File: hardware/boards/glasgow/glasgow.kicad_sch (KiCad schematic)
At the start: 95 parts, among them J1 USB_C_USB2.0, SW1 RST, U1 CY7C68013A-56LTX, U15 TPD3S014, U2 CAT24M01X, U3 BL24C256A-SFRC, U30 ICE40HX8K-BG121, U36 TLV73312PQDRVR, U7 APX811-40UG-7, U8 TLV75533PDRVR, Y1 24M

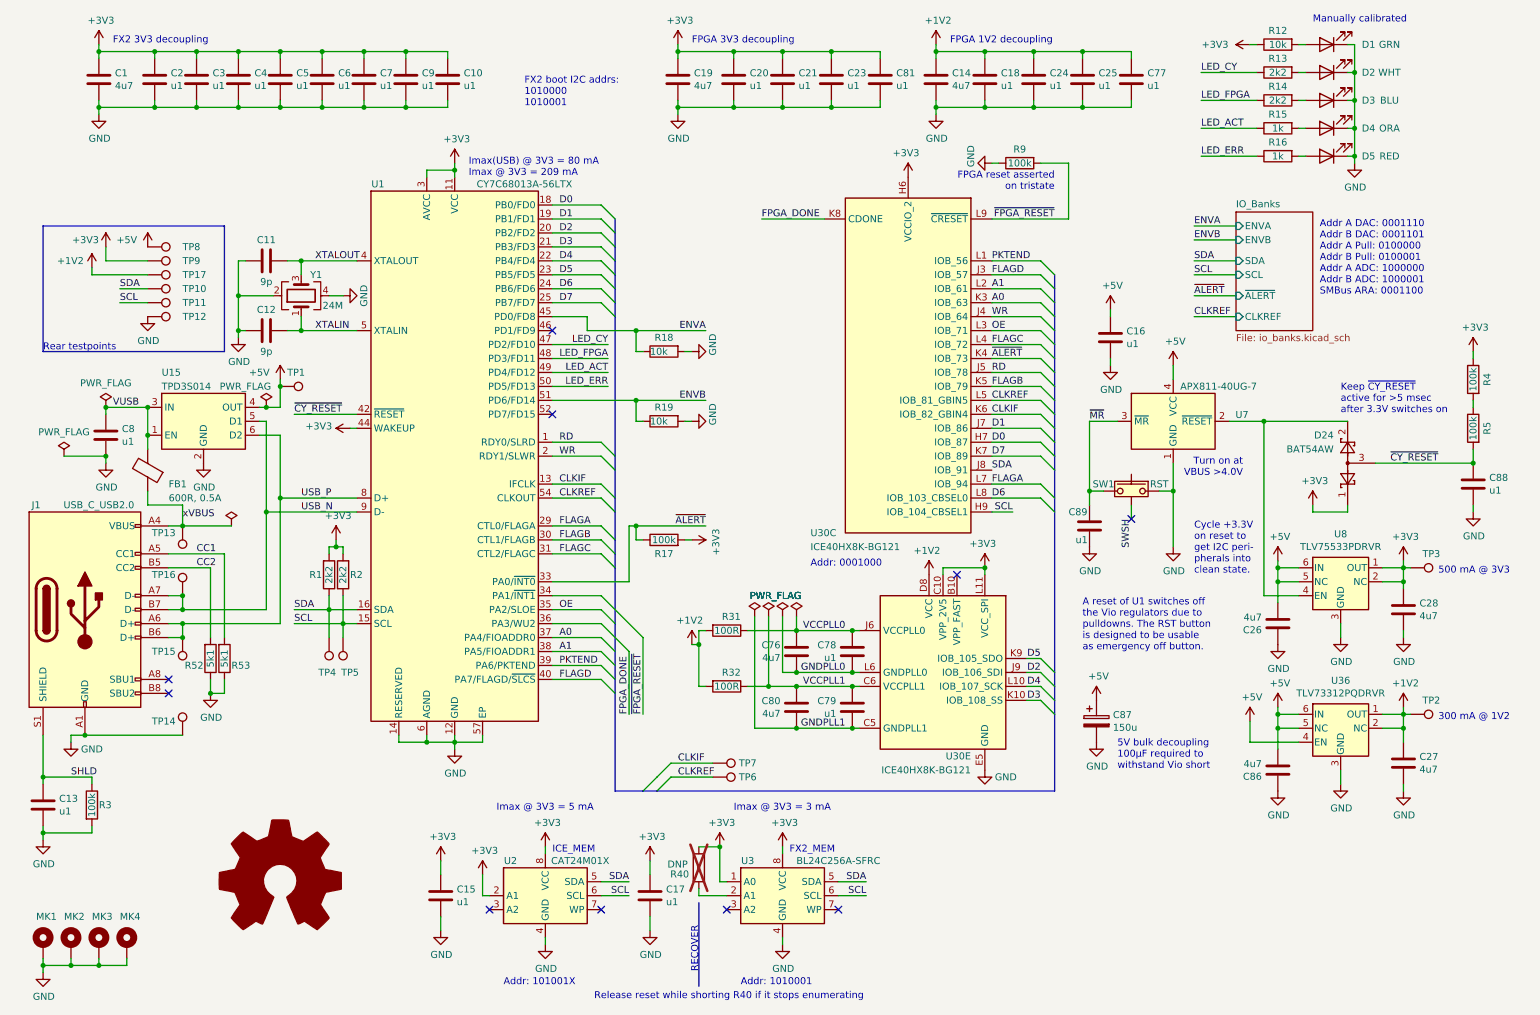
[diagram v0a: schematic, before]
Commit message: Remove one of the sides
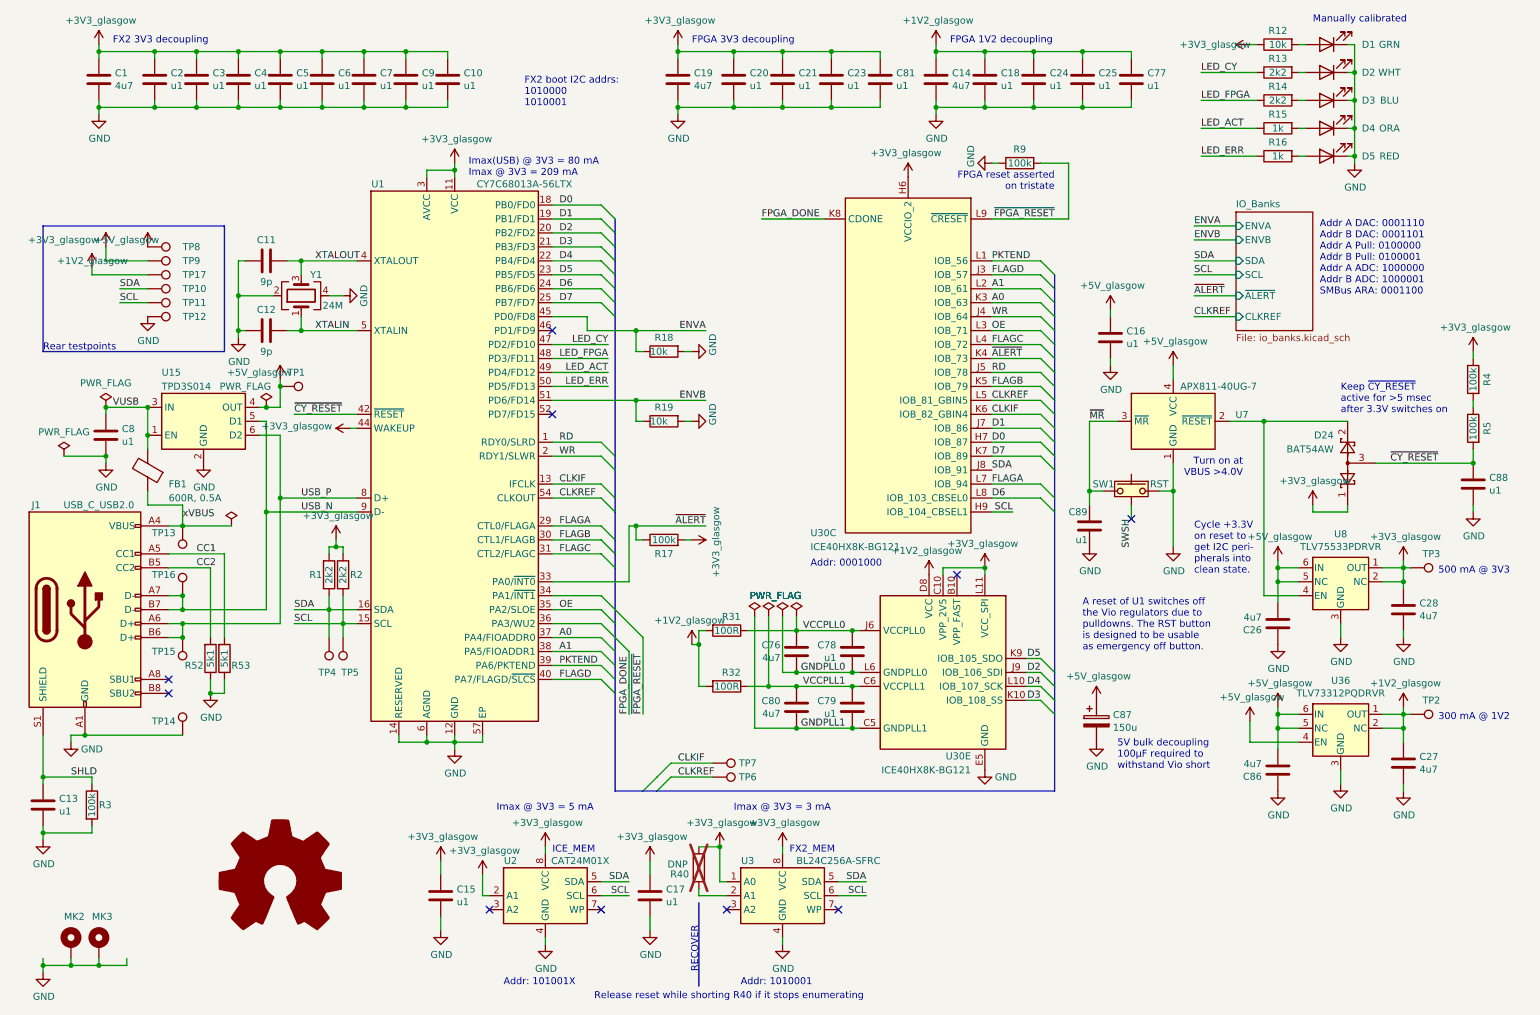
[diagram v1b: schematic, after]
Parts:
- removed MK1, MK4: Mounting_Hole_PAD, Glasgow:MountingHole_3.5mm_Pad_Via_CrtYd, symbol Mechanical:MountingHole_Pad
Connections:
- net +1V2 renamed +1V2_glasgow
- net +3V3 renamed +3V3_glasgow
- net +5V renamed +5V_glasgow
